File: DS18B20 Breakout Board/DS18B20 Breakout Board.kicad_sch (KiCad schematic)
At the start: 3 parts, among them J1 Conn_01x02_Socket, J2 Conn_01x02_Socket, U1 DS18B20

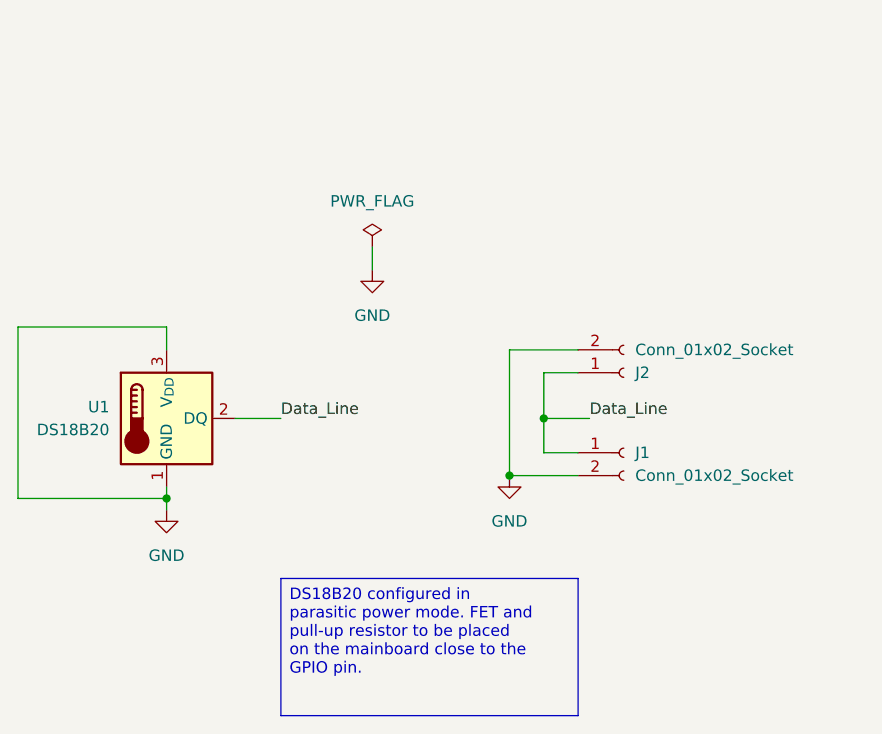
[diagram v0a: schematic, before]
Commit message: reconfigure DS18B20 breakout board
- Change JST from 2-pin to 3-pin
- Add a solder jumper for switching between parasitic and external power
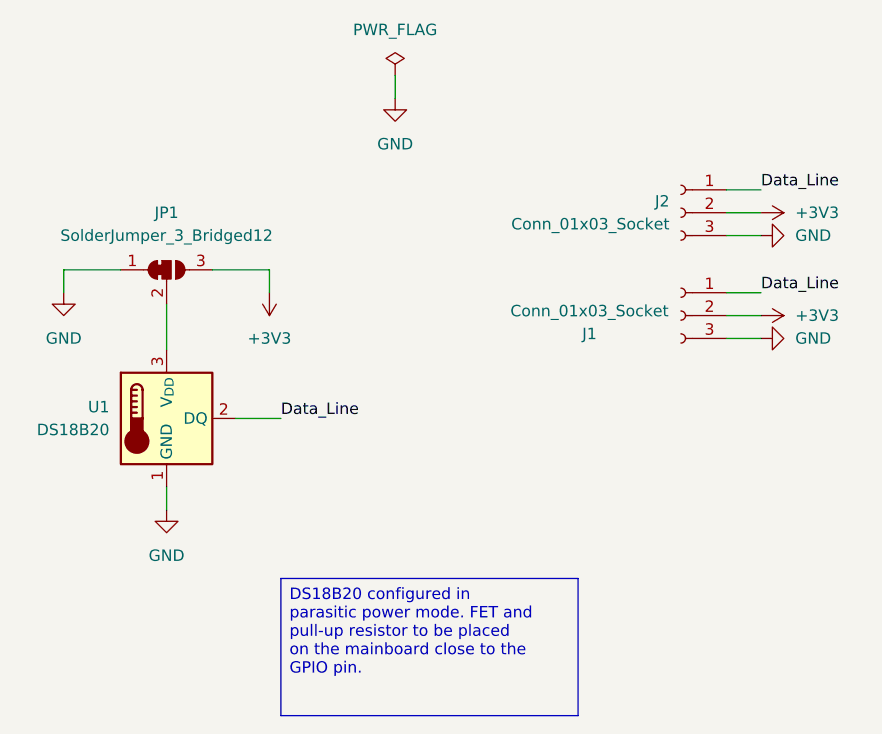
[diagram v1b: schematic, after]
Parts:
- removed J1, J2: Conn_01x02_Socket, Connector_PinHeader_2.54mm:PinHeader_1x02_P2.54mm_Vertical, symbol Connector:Conn_01x02_Socket
- added J1, J2: Conn_01x03_Socket, Connector_PinSocket_2.54mm:PinSocket_1x03_P2.54mm_Vertical, symbol Connector:Conn_01x03_Socket
- added JP1: SolderJumper_3_Bridged12, Jumper:SolderJumper-3_P1.3mm_Bridged12_RoundedPad1.0x1.5mm_NumberLabels, symbol Jumper:SolderJumper_3_Bridged12
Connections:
- net Data_Line: now also J1.1 (Pin_1), J2.1 (Pin_1)
- net GND: now also J1.3 (Pin_3), J2.3 (Pin_3), JP1.1 (A); no longer U1.3 (V_{DD})
- new net: JP1.2 (C), U1.3 (V_{DD})
- new net +3V3: J1.2 (Pin_2), J2.2 (Pin_2), JP1.3 (B)
